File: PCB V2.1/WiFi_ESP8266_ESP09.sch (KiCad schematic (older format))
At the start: 0 parts

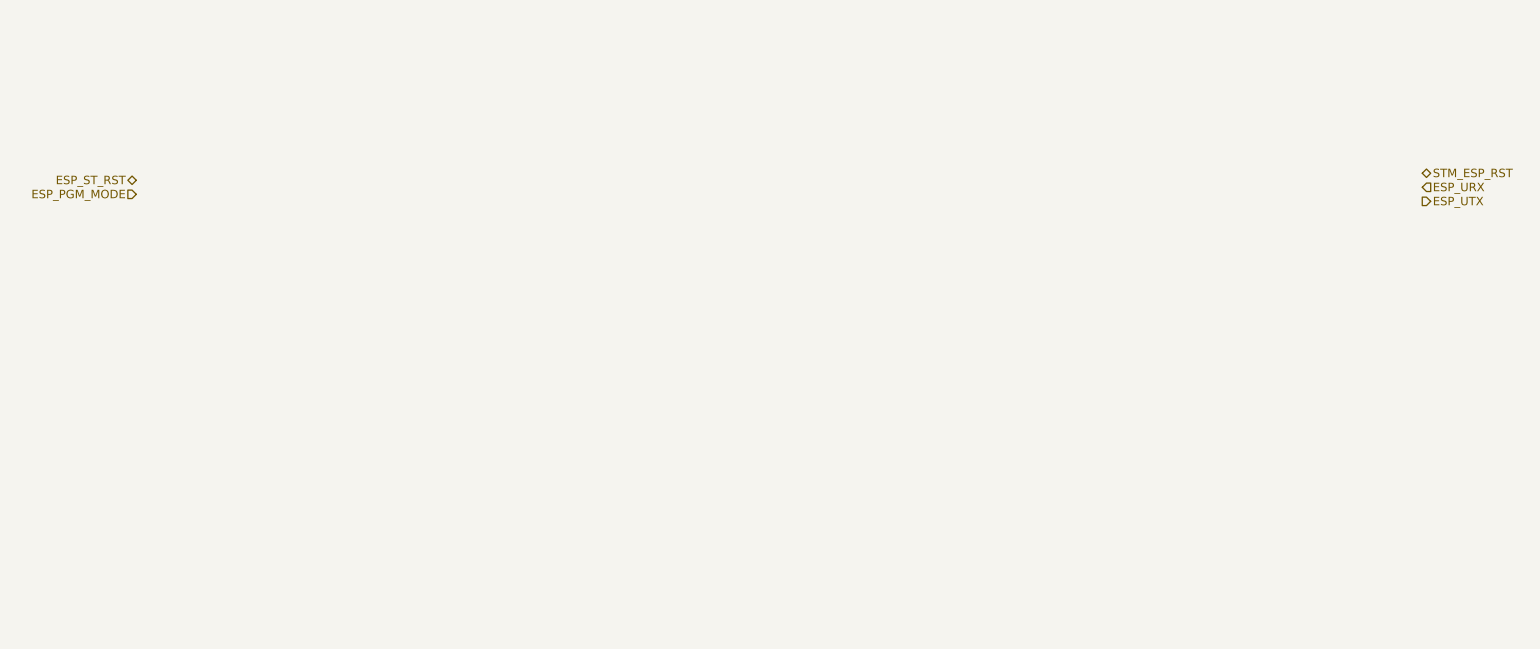
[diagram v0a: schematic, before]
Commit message: SunLeaf Alpha 0.2 and KiCAD Port
SunLeaf rev 2 called Alhpa 0.2 or 0.2a is the main component of this
commit. The entire hardware project has been ported to KiCAD libaries
and all. 0.2a features a revised formfactor, better ESP module, and many
fixes over the original. This version will also be capable of OTA
updates.
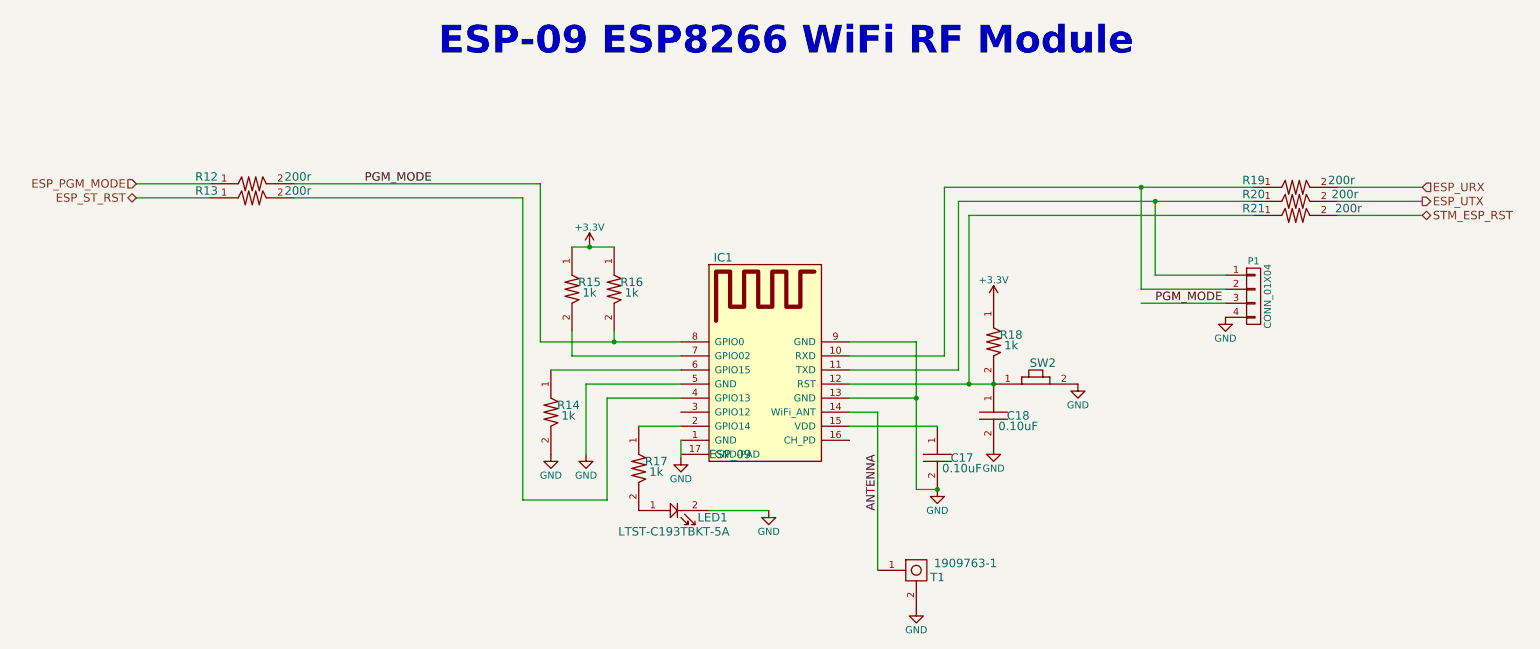
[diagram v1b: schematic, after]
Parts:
- added C17, C18: CL05B104JP5NNNC, PCB_Footprints:C0402, symbol CL05B104JP5NNNC
- added IC1: ESP_09, PCB_Footprints:ESP-09, symbol ESP_09
- added LED1: LTST-C193TBKT-5A, PCB_Footprints:LED0603, symbol LTST-C193TBKT-5A
- added P1: CONN_01X04, Pin_Headers:Pin_Header_Straight_1x04, symbol CONN_01X04
- added R12, R13, R19, R20, R21: RC1005F201CS, PCB_Footprints:R0402, symbol RC1005F201CS
- added R14, R15, R16, R17, R18: RC1005F102CS, PCB_Footprints:R0402, symbol RC1005F102CS
- added SW2: B3U-1000P, PCB_Footprints:B3U-1000P, symbol B3U-1000P
- added T1: 1909763-1, PCB_Footprints:1909763-1, symbol 1909763-1
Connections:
- net ESP_PGM_MODE: now also R12.1
- net ESP_ST_RST: now also R13.1
- net ESP_URX: now also R19.2
- net ESP_UTX: now also R20.2
- net STM_ESP_RST: now also R21.2
- new net: IC1.10 (RXD), P1.2 (P2), R19.1
- new net: IC1.11 (TXD), P1.1 (P1), R20.1
- new net: C18.1, IC1.12 (RST), R18.2, R21.1, SW2.1
- new net: C17.1, IC1.15 (VDD)
- new net: IC1.2 (GPIO14), R17.1
- new net: IC1.4 (GPIO13), R13.2
- new net: IC1.6 (GPIO15), R14.1
- new net: IC1.7 (GPIO02), R15.2
- new net: LED1.1, R17.2
- new net +3V3: R15.1, R16.1, R18.1
- new net ANTENNA: IC1.14 (WiFi_ANT), T1.1
- new net GND: C17.2, C18.2, IC1.1 (GND), IC1.13 (GND), IC1.5 (GND), IC1.9 (GND), LED1.2, P1.4 (P4), R14.2, SW2.2, T1.2
- new net PGM_MODE: IC1.8 (GPIO0), P1.3 (P3), R12.2, R16.2
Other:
- note added: "ESP-09 ESP8266 WiFi RF Module"

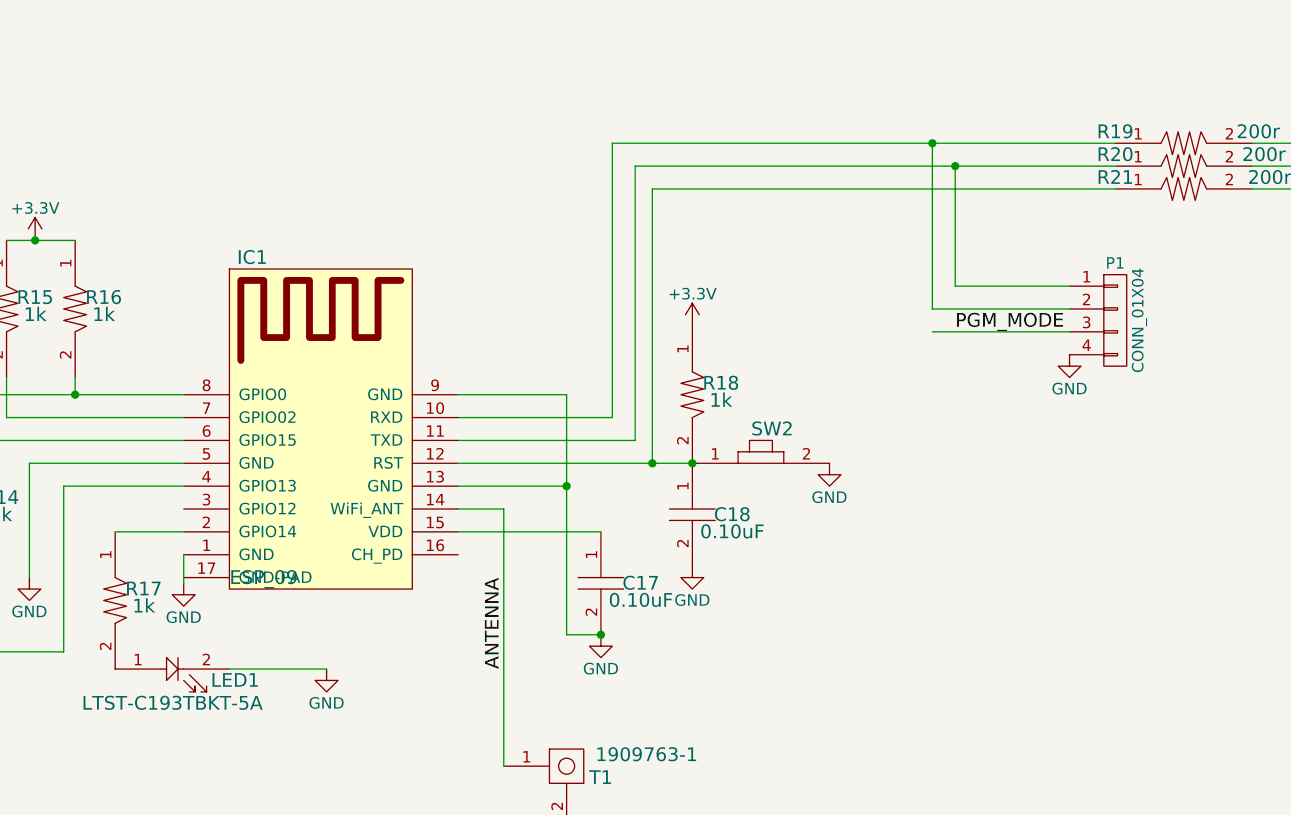
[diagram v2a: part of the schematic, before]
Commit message: Placement
Heavy progress on component placement in KiCAD for SunLEaf V2,
committing to save progress, nightly builds of KiCAD are very crash
prone.
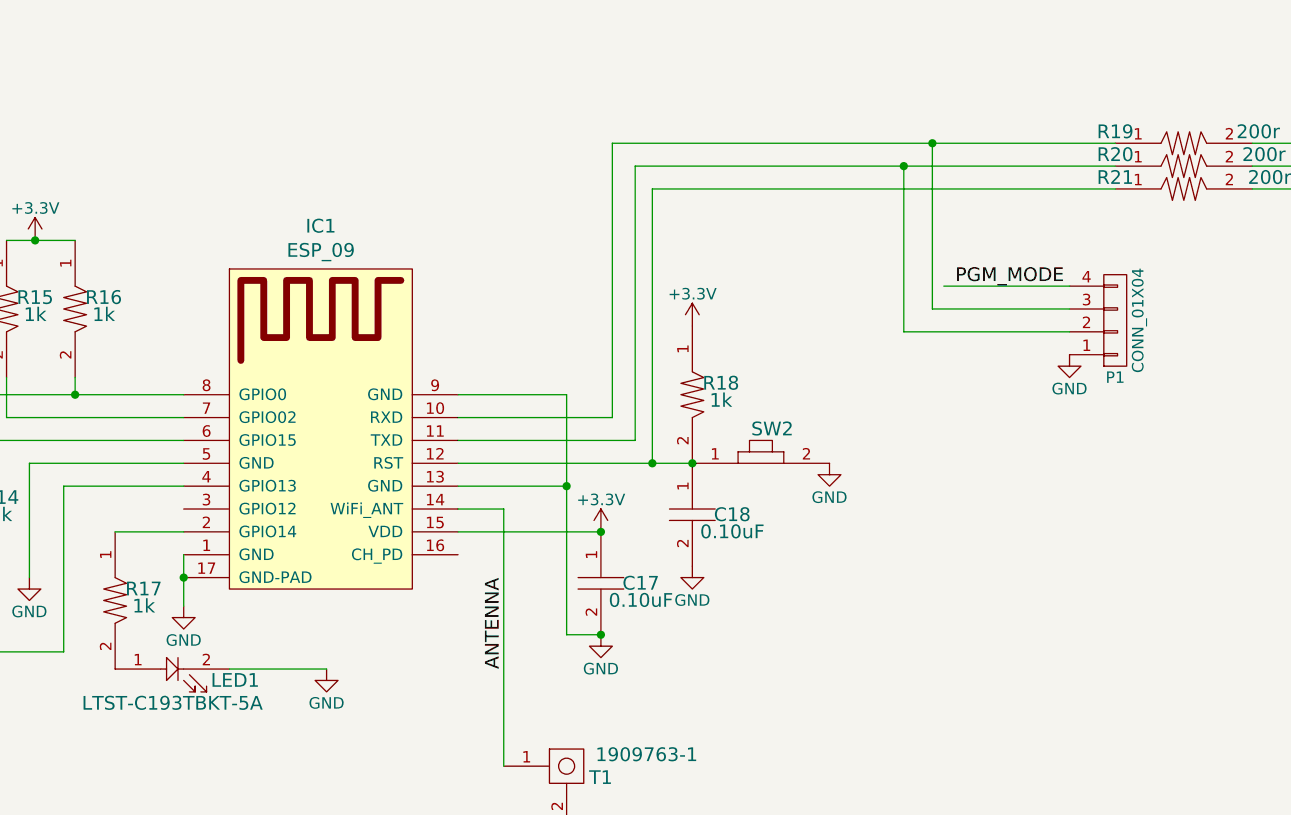
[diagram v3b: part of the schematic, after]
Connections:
- net +3V3: now also C17.1, IC1.15 (VDD)
- net GND: now also IC1.17 (GND-PAD), P1.1 (P1); no longer P1.4 (P4)
- net PGM_MODE: now also P1.4 (P4); no longer P1.3 (P3)
- net at IC1.10 (RXD), R19.1: now also P1.3 (P3); no longer P1.2 (P2)
- net at IC1.11 (TXD), R20.1: now also P1.2 (P2); no longer P1.1 (P1)
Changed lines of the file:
@@
 ESP_PGM_MODE
-$Comp
-L ESP_09 IC1
-U 1 1 57D6FE85
-P 5825 3650
-F 0 "IC1" H 5525 4650 60  0000 C CNN
-F 1 "ESP_09" H 5575 3250 60  0000 C CNN
-F 2 "PCB_Footprints:ESP-09" H 7225 4250 60  0001 C CNN
-F 3 "" H 7225 4250 60  0001 C CNN
-	1    5825 3650
-	1    0    0    -1
-$EndComp
 $Comp
 L B3U-1000P SW2
@@
 $EndComp
 $Comp
-L GND #PWR24
+L GND #PWR26
 U 1 1 57D74187
 P 7050 4300
-F 0 "#PWR24" H 7050 4050 50  0001 C CNN
+F 0 "#PWR26" H 7050 4050 50  0001 C CNN
 F 1 "GND" H 7050 4150 50  0000 C CNN
 F 2 "" H 7050 4300 50  0000 C CNN
@@
 $EndComp
 $Comp
-L GND #PWR27
+L GND #PWR29
 U 1 1 57D744DC
 P 8050 3550
-F 0 "#PWR27" H 8050 3300 50  0001 C CNN
+F 0 "#PWR29" H 8050 3300 50  0001 C CNN
 F 1 "GND" H 8050 3400 50  0000 C CNN
 F 2 "" H 8050 3550 50  0000 C CNN
@@
 $EndComp
 $Comp
-L GND #PWR26
+L GND #PWR28
 U 1 1 57D745DC
 P 7450 4000
-F 0 "#PWR26" H 7450 3750 50  0001 C CNN
+F 0 "#PWR28" H 7450 3750 50  0001 C CNN
 F 1 "GND" H 7450 3850 50  0000 C CNN
 F 2 "" H 7450 4000 50  0000 C CNN
@@
 $EndComp
 $Comp
-L GND #PWR23
+L GND #PWR24
 U 1 1 57D74617
 P 6900 5150
-F 0 "#PWR23" H 6900 4900 50  0001 C CNN
+F 0 "#PWR24" H 6900 4900 50  0001 C CNN
 F 1 "GND" H 6900 5000 50  0000 C CNN
 F 2 "" H 6900 5150 50  0000 C CNN
@@
 $EndComp
 $Comp
-L +3.3V #PWR25
+L +3.3V #PWR27
 U 1 1 57D7466A
 P 7450 2950
-F 0 "#PWR25" H 7450 2800 50  0001 C CNN
+F 0 "#PWR27" H 7450 2800 50  0001 C CNN
 F 1 "+3.3V" H 7450 3090 50  0000 C CNN
 F 2 "" H 7450 2950 50  0000 C CNN
@@
 $EndComp
 $Comp
-L GND #PWR18
+L GND #PWR19
 U 1 1 57D76DFD
 P 4300 4050
-F 0 "#PWR18" H 4300 3800 50  0001 C CNN
+F 0 "#PWR19" H 4300 3800 50  0001 C CNN
 F 1 "GND" H 4300 3900 50  0000 C CNN
 F 2 "" H 4300 4050 50  0000 C CNN
@@
 $EndComp
 $Comp
-L GND #PWR21
+L GND #PWR22
 U 1 1 57D76E32
-P 5225 4075
-F 0 "#PWR21" H 5225 3825 50  0001 C CNN
-F 1 "GND" H 5225 3925 50  0000 C CNN
-F 2 "" H 5225 4075 50  0000 C CNN
-F 3 "" H 5225 4075 50  0000 C CNN
-	1    5225 4075
-	1    0    0    -1
-$EndComp
-$Comp
-L GND #PWR19
+P 5225 4175
+F 0 "#PWR22" H 5225 3925 50  0001 C CNN
+F 1 "GND" H 5225 4025 50  0000 C CNN
+F 2 "" H 5225 4175 50  0000 C CNN
+F 3 "" H 5225 4175 50  0000 C CNN
+	1    5225 4175
+	1    0    0    -1
+$EndComp
+$Comp
+L GND #PWR20
 U 1 1 57D76FA5
 P 4550 4050
-F 0 "#PWR19" H 4550 3800 50  0001 C CNN
+F 0 "#PWR20" H 4550 3800 50  0001 C CNN
 F 1 "GND" H 4550 3900 50  0000 C CNN
 F 2 "" H 4550 4050 50  0000 C CNN
@@
 $EndComp
 $Comp
-L +3.3V #PWR20
+L +3.3V #PWR21
 U 1 1 57D77481
 P 4575 2575
-F 0 "#PWR20" H 4575 2425 50  0001 C CNN
+F 0 "#PWR21" H 4575 2425 50  0001 C CNN
 F 1 "+3.3V" H 4575 2715 50  0000 C CNN
 F 2 "" H 4575 2575 50  0000 C CNN
@@
 $EndComp
 $Comp
-L GND #PWR22
+L GND #PWR23
 U 1 1 57D7A082
 P 5850 4450
-F 0 "#PWR22" H 5850 4200 50  0001 C CNN
+F 0 "#PWR23" H 5850 4200 50  0001 C CNN
 F 1 "GND" H 5850 4300 50  0000 C CNN
 F 2 "" H 5850 4450 50  0000 C CNN
@@
 F 3 "" H 9300 2925 50  0000 C CNN
 	1    9300 2925
-	1    0    0    -1
-$EndComp
-Wire Wire Line
-	6425 3850 7050 3850
-Wire Wire Line
-	6425 3650 6900 3650
-Wire Wire Line
-	6900 3250 6900 4300
-Wire Wire Line
-	6900 4300 7050 4300
-Connection ~ 7050 4300
-Wire Wire Line
-	6425 3250 6900 3250
-Connection ~ 6900 3650
-Wire Wire Line
-	6425 3550 7450 3550
-Connection ~ 7450 3550
-Wire Wire Line
-	6425 3750 6625 3750
-Wire Wire Line
-	6625 3750 6625 4875
-Wire Wire Line
-	6425 3350 7100 3350
-Wire Wire Line
-	7100 3350 7100 2150
-Wire Wire Line
-	6425 3450 7200 3450
-Wire Wire Line
-	7200 3450 7200 2250
-Wire Wire Line
-	7275 2350 7275 3550
-Connection ~ 7275 3550
-Wire Wire Line
-	10500 2150 9900 2150
-Wire Wire Line
-	7100 2150 9300 2150
-Wire Wire Line
-	9900 2250 10500 2250
-Wire Wire Line
-	10500 2350 9900 2350
-Wire Wire Line
-	7200 2250 9300 2250
-Wire Wire Line
-	7275 2350 9300 2350
-Wire Wire Line
-	1350 2125 1875 2125
-Wire Wire Line
-	1350 2225 1875 2225
-Wire Wire Line
-	2475 2125 4225 2125
-Wire Wire Line
-	4225 2125 4225 3250
-Wire Wire Line
-	4225 3250 5225 3250
-Wire Wire Line
-	4450 3175 4450 3350
-Wire Wire Line
-	4450 3350 5225 3350
-Wire Wire Line
-	4750 3175 4750 3250
-Connection ~ 4750 3250
-Wire Wire Line
-	5225 3450 4300 3450
-Wire Wire Line
-	5225 3950 5225 4075
-Wire Wire Line
-	5225 3550 4550 3550
-Wire Wire Line
-	4550 3550 4550 4050
-Wire Wire Line
-	5225 3650 4700 3650
-Wire Wire Line
-	4700 3650 4700 4375
-Wire Wire Line
-	4700 4375 4100 4375
-Wire Wire Line
-	4100 4375 4100 2225
-Wire Wire Line
-	4100 2225 2475 2225
-Wire Wire Line
-	4450 2575 4750 2575
-Connection ~ 4575 2575
-Wire Wire Line
-	5850 4450 5425 4450
-Wire Wire Line
-	5225 3850 4925 3850
-Wire Wire Line
-	9100 2875 8500 2875
-Wire Wire Line
-	8500 2875 8500 2150
-Connection ~ 8500 2150
-Wire Wire Line
-	9100 2775 8600 2775
-Wire Wire Line
-	8600 2775 8600 2250
-Connection ~ 8600 2250
-$Comp
-L GND #PWR28
+	1    0    0    1
+$EndComp
+$Comp
+L GND #PWR30
 U 1 1 57D7BD68
 P 9100 3075
-F 0 "#PWR28" H 9100 2825 50  0001 C CNN
+F 0 "#PWR30" H 9100 2825 50  0001 C CNN
 F 1 "GND" H 9100 2925 50  0000 C CNN
 F 2 "" H 9100 3075 50  0000 C CNN
@@
 	1    0    0    -1
 $EndComp
-Wire Wire Line
-	9100 2975 8500 2975
-Text Label 8600 2975 0    60   ~ 0
+Text Label 8600 2775 0    60   ~ 0
 PGM_MODE
 Text Label 2975 2125 0    60   ~ 0
@@
 Text Notes 3500 1225 0    197  ~ 39
 ESP-09 ESP8266 WiFi RF Module
+$Comp
+L +3.3V #PWR25
+U 1 1 57D94D09
+P 7050 3850
+F 0 "#PWR25" H 7050 3700 50  0001 C CNN
+F 1 "+3.3V" H 7050 3990 50  0000 C CNN
+F 2 "" H 7050 3850 50  0000 C CNN
+F 3 "" H 7050 3850 50  0000 C CNN
+	1    7050 3850
+	1    0    0    -1
+$EndComp
+$Comp
+L ESP_09 IC1
+U 1 1 57DA529A
+P 5825 3650
+F 0 "IC1" H 5825 4787 60  0000 C CNN
+F 1 "ESP_09" H 5825 4681 60  0000 C CNN
+F 2 "PCB_Footprints:ESP-09" H 7225 4250 60  0001 C CNN
+F 3 "" H 7225 4250 60  0001 C CNN
+	1    5825 3650
+	1    0    0    -1
+$EndComp
+Wire Wire Line
+	9100 2775 8550 2775
+Connection ~ 8375 2250
+Wire Wire Line
+	8375 2975 8375 2250
+Wire Wire Line
+	9100 2975 8375 2975
+Connection ~ 5225 4050
+Connection ~ 7050 3850
+Connection ~ 8500 2150
+Wire Wire Line
+	8500 2875 8500 2150
+Wire Wire Line
+	9100 2875 8500 2875
+Wire Wire Line
+	5225 3850 4925 3850
+Wire Wire Line
+	5850 4450 5425 4450
+Connection ~ 4575 2575
+Wire Wire Line
+	4450 2575 4750 2575
+Wire Wire Line
+	4100 2225 2475 2225
+Wire Wire Line
+	4100 4375 4100 2225
+Wire Wire Line
+	4700 4375 4100 4375
+Wire Wire Line
+	4700 3650 4700 4375
+Wire Wire Line
+	5225 3650 4700 3650
+Wire Wire Line
+	4550 3550 4550 4050
+Wire Wire Line
+	5225 3550 4550 3550
+Wire Wire Line
+	5225 3950 5225 4175
+Wire Wire Line
+	5225 3450 4300 3450
+Connection ~ 4750 3250
+Wire Wire Line
+	4750 3175 4750 3250
+Wire Wire Line
+	4450 3350 5225 3350
+Wire Wire Line
+	4450 3175 4450 3350
+Wire Wire Line
+	4225 3250 5225 3250
+Wire Wire Line
+	4225 2125 4225 3250
+Wire Wire Line
+	2475 2125 4225 2125
+Wire Wire Line
+	1350 2225 1875 2225
+Wire Wire Line
+	1350 2125 1875 2125
+Wire Wire Line
+	7275 2350 9300 2350
+Wire Wire Line
+	7200 2250 9300 2250
+Wire Wire Line
+	10500 2350 9900 2350
+Wire Wire Line
+	9900 2250 10500 2250
+Wire Wire Line
+	7100 2150 9300 2150
+Wire Wire Line
+	10500 2150 9900 2150
+Connection ~ 7275 3550
+Wire Wire Line
+	7275 2350 7275 3550
+Wire Wire Line
+	7200 3450 7200 2250
+Wire Wire Line
+	6425 3450 7200 3450
+Wire Wire Line
+	7100 3350 7100 2150
+Wire Wire Line
+	6425 3350 7100 3350
+Wire Wire Line
+	6625 3750 6625 4875
+Wire Wire Line
+	6425 3750 6625 3750
+Connection ~ 7450 3550
+Wire Wire Line
+	6425 3550 7450 3550
+Connection ~ 6900 3650
+Wire Wire Line
+	6425 3250 6900 3250
+Connection ~ 7050 4300
+Wire Wire Line
+	6900 4300 7050 4300
+Wire Wire Line
+	6900 3250 6900 4300
+Wire Wire Line
+	6425 3650 6900 3650
+Wire Wire Line
+	6425 3850 7050 3850
 $EndSCHEMATC
